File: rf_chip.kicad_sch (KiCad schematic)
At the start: 8 parts, among them IC4 DW3120TR13, Y1 ECS-384-CDX-2482

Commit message: SPI for rf chip DW and MCU, finding a SP8T or SP4T
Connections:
- net DW_SPIDO renamed DW_SPIMISO
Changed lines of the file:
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@@
     )
   )
-  (global_label "DW_SPIDO" (shape bidirectional) (at 48.26 43.18 180) (fields_autoplaced)
+  (global_label "DW_SPIMISO" (shape bidirectional) (at 48.26 43.18 180) (fields_autoplaced)
     (effects (font (size 1.27 1.27)) (justify right))
-    (property "Intersheetrefs" "${INTERSHEET_REFS}" (at 34.7897 43.18 0)
+    (property "Intersheetrefs" "${INTERSHEET_REFS}" (at 32.794 43.18 0)
       (effects (font (size 1.27 1.27)) (justify right) hide)
     )

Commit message: adding all footprints moving onto pcb
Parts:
- C50, C51, C54, C55: footprint (none) -> Capacitor_SMD:C_0603_1608Metric
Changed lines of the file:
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@@
       (effects (font (size 1.27 1.27)) (justify left))
     )
-    (property "Footprint" "" (at 193.04 48.26 0)
+    (property "Footprint" "Capacitor_SMD:C_0603_1608Metric" (at 193.04 48.26 0)
       (effects (font (size 1.27 1.27)) hide)
     )
@@
       (effects (font (size 1.27 1.27)) (justify left))
     )
-    (property "Footprint" "" (at 29.21 29.21 0)
+    (property "Footprint" "Capacitor_SMD:C_0603_1608Metric" (at 29.21 29.21 0)
       (effects (font (size 1.27 1.27)) hide)
     )
@@
       (effects (font (size 1.27 1.27)) (justify right))
     )
-    (property "Footprint" "" (at 210.82 50.8 0)
+    (property "Footprint" "Capacitor_SMD:C_0603_1608Metric" (at 210.82 50.8 0)
       (effects (font (size 1.27 1.27)) hide)
     )
@@
       (effects (font (size 1.27 1.27)) (justify right))
     )
-    (property "Footprint" "" (at 29.21 96.52 0)
+    (property "Footprint" "Capacitor_SMD:C_0603_1608Metric" (at 29.21 96.52 0)
       (effects (font (size 1.27 1.27)) hide)
     )

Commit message: fixed GS_VBUS overtaking the GND symbol error, lesson learned, fixed PCB ratnest
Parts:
- removed AE1, AE2: Antenna, symbol Device:Antenna
- IC4: footprint DW3120TR13 -> dw3120:DW3120TR13
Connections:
- net DW_RF2: now reaches IC4.H11 (RF1)
- net DW_RF1: now reaches IC4.H5 (RF2)
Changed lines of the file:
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@@
+    )
+  )
+  (global_label "DW_RF1" (shape bidirectional) (at 139.7 88.9 0) (fields_autoplaced)
+    (effects (font (size 1.27 1.27)) (justify left))
+    (property "Intersheetrefs" "${INTERSHEET_REFS}" (at 151.0536 88.9 0)
+      (effects (font (size 1.27 1.27)) (justify left) hide)
     )
   )
@@
     (property "Intersheetrefs" "${INTERSHEET_REFS}" (at 36.0597 96.52 0)
       (effects (font (size 1.27 1.27)) (justify right) hide)
+    )
+  )
+  (global_label "DW_RF2" (shape bidirectional) (at 144.78 96.52 0) (fields_autoplaced)
+    (effects (font (size 1.27 1.27)) (justify left))
+    (property "Intersheetrefs" "${INTERSHEET_REFS}" (at 156.1336 96.52 0)
+      (effects (font (size 1.27 1.27)) (justify left) hide)
     )
   )
@@
     )
   )
-  (symbol (lib_id "Device:Antenna") (at 144.78 91.44 0) (unit 1)
-    (in_bom yes) (on_board yes) (dnp no) (fields_autoplaced)
-    (property "Reference" "AE2" (at 147.32 90.805 0)
-      (effects (font (size 1.27 1.27)) (justify left))
-    )
-    (property "Value" "Antenna" (at 147.32 93.345 0)
-      (effects (font (size 1.27 1.27)) (justify left))
-    )
-    (property "Footprint" "" (at 144.78 91.44 0)
-      (effects (font (size 1.27 1.27)) hide)
-    )
-    (property "Datasheet" "~" (at 144.78 91.44 0)
-      (effects (font (size 1.27 1.27)) hide)
-    )
-    (pin "1")
-    (instances
-      (project "radar2"
-        (path "/4b235fed-a05d-46ae-99fd-4a907d865754/40342fd5-2d07-4fe2-a926-1f2842abe411"
-          (reference "AE2") (unit 1)
-        )
-      )
-    )
-  )
   (symbol (lib_id "power:GND") (at 29.21 33.02 0) (unit 1)
     (in_bom yes) (on_board yes) (dnp no) (fields_autoplaced)
@@
     )
   )
-  (symbol (lib_id "Device:Antenna") (at 139.7 83.82 0) (unit 1)
-    (in_bom yes) (on_board yes) (dnp no) (fields_autoplaced)
-    (property "Reference" "AE1" (at 142.24 83.185 0)
-      (effects (font (size 1.27 1.27)) (justify left))
-    )
-    (property "Value" "Antenna" (at 142.24 85.725 0)
-      (effects (font (size 1.27 1.27)) (justify left))
-    )
-    (property "Footprint" "" (at 139.7 83.82 0)
-      (effects (font (size 1.27 1.27)) hide)
-    )
-    (property "Datasheet" "~" (at 139.7 83.82 0)
-      (effects (font (size 1.27 1.27)) hide)
-    )
-    (pin "1")
-    (instances
-      (project "radar2"
-        (path "/4b235fed-a05d-46ae-99fd-4a907d865754/40342fd5-2d07-4fe2-a926-1f2842abe411"
-          (reference "AE1") (unit 1)
-        )
-      )
-    )
-  )
   (symbol (lib_id "power:GND") (at 120.65 109.22 0) (unit 1)
     (in_bom yes) (on_board yes) (dnp no) (fields_autoplaced)
@@
       (effects (font (size 1.27 1.27)))
     )
-    (property "Footprint" "DW3120TR13" (at 115.57 133.02 0)
+    (property "Footprint" "dw3120:DW3120TR13" (at 115.57 133.02 0)
       (effects (font (size 1.27 1.27)) (justify left top) hide)
     )

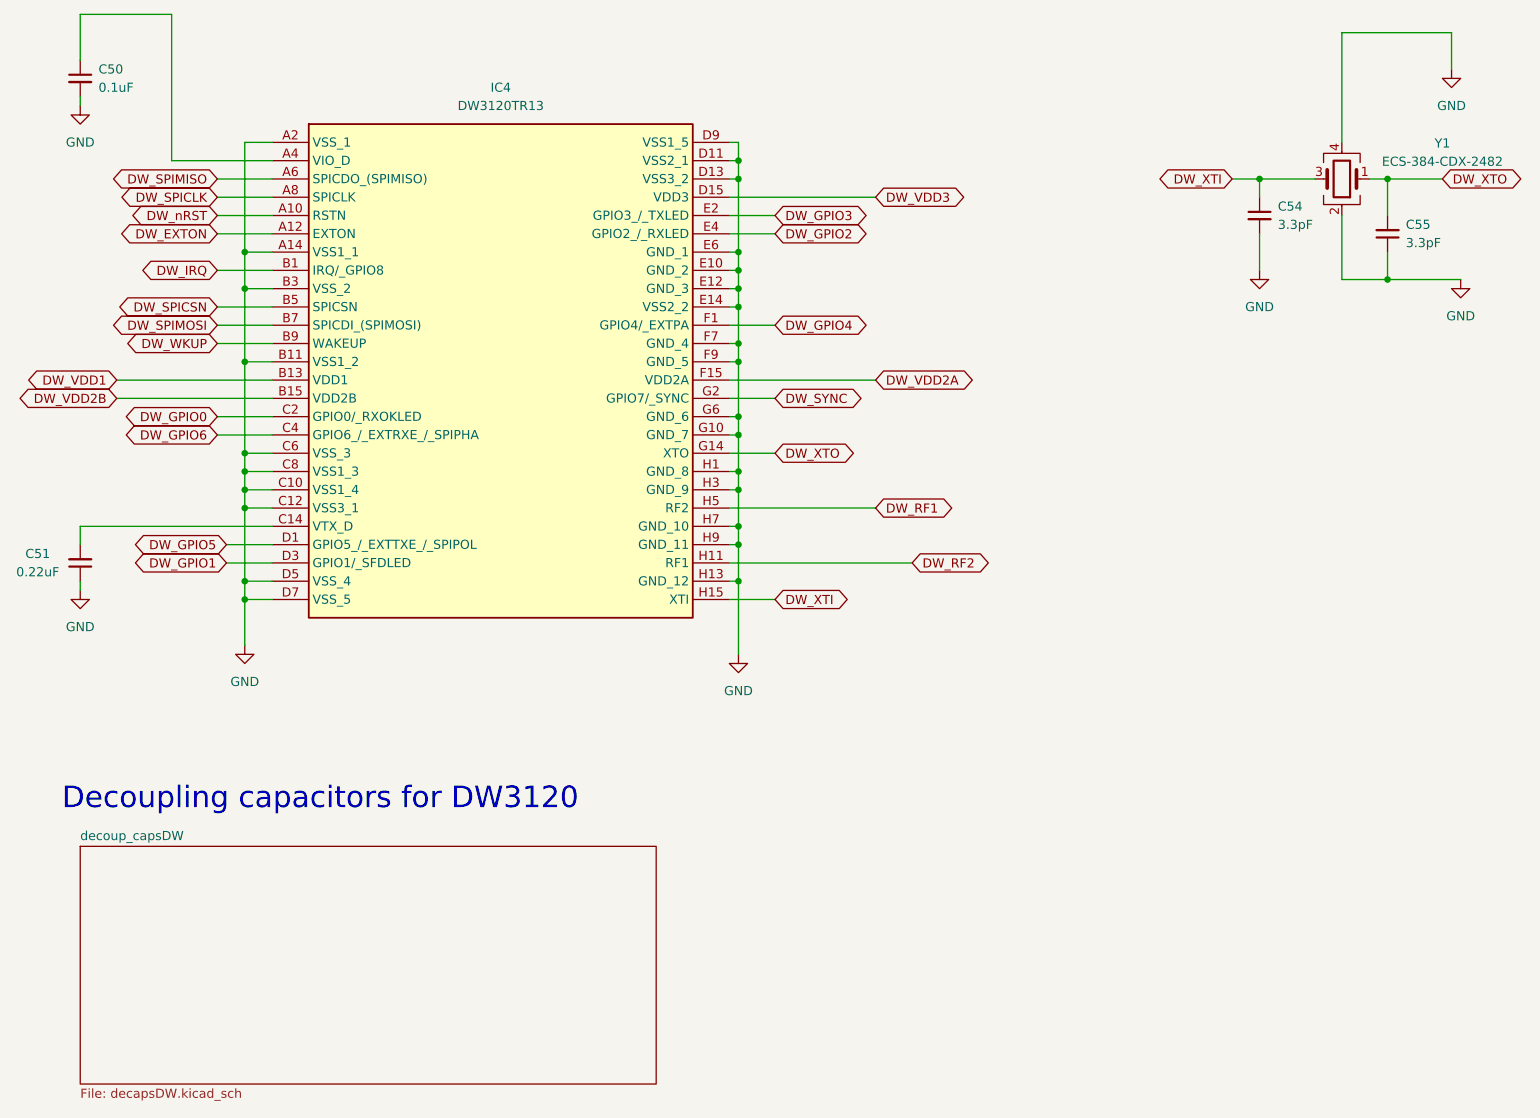
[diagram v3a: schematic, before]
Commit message: adding the .stp files for 3d viewer
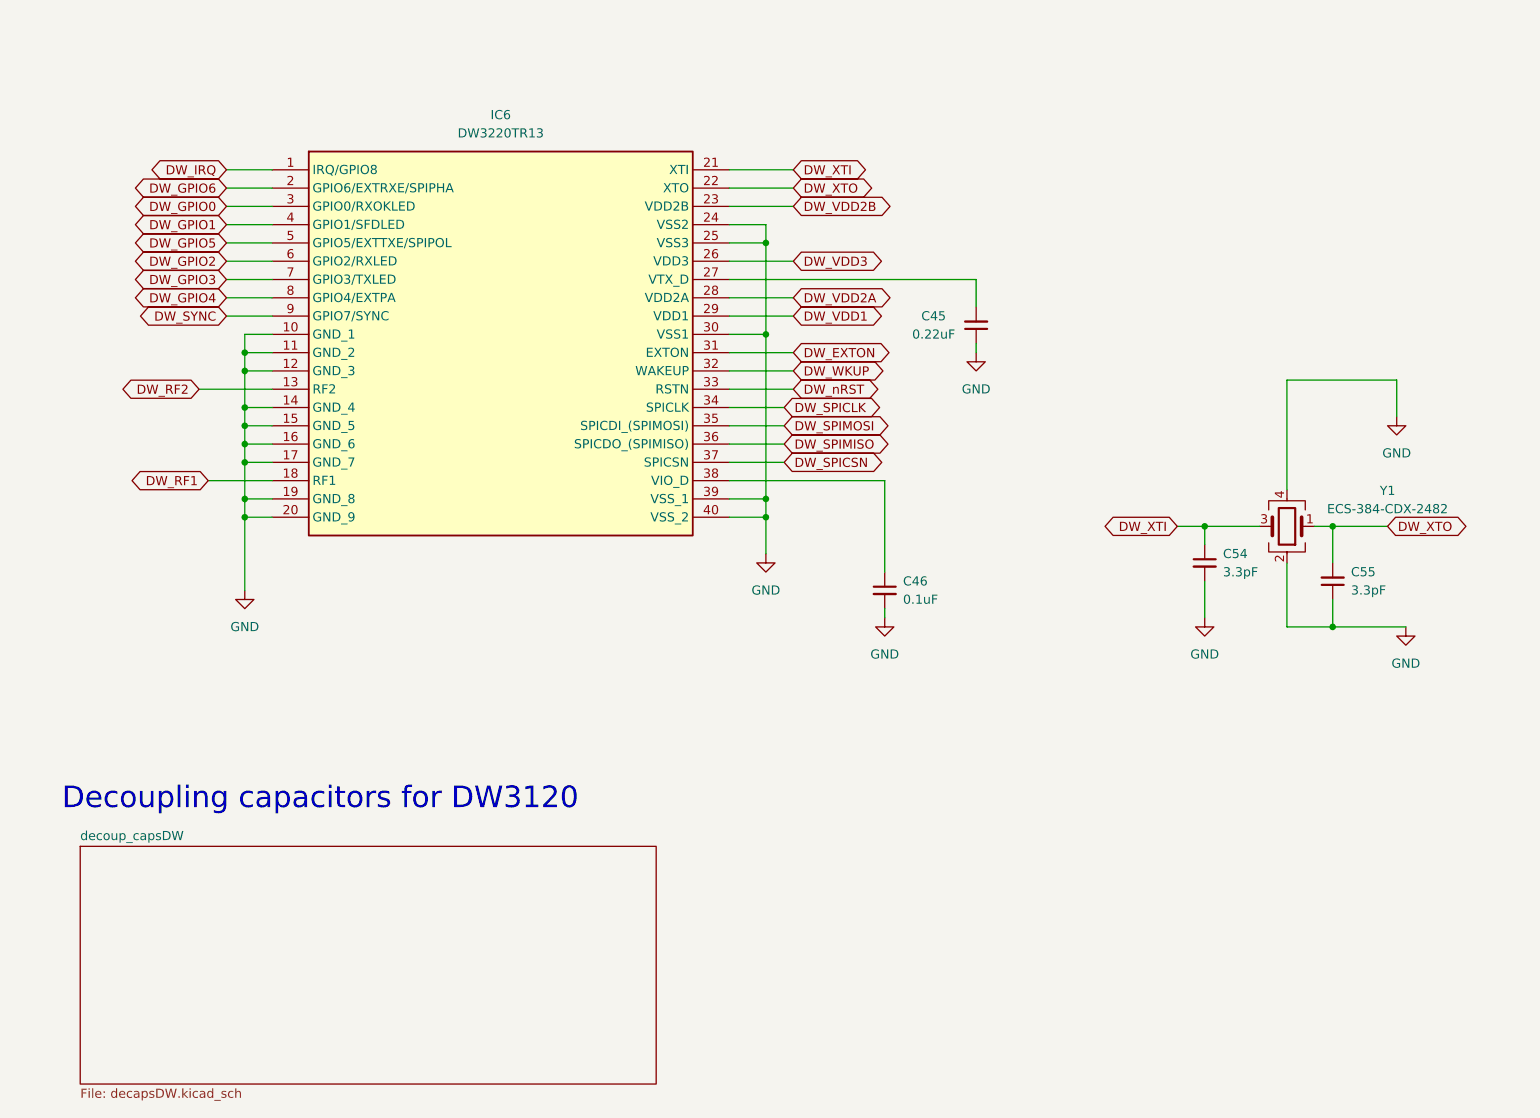
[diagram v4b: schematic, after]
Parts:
- removed C50: 0.1uF, Capacitor_SMD:C_0603_1608Metric, symbol Device:C_Small
- removed C51: 0.22uF, Capacitor_SMD:C_0603_1608Metric, symbol Device:C_Small
- removed IC4: DW3120TR13, dw3120:DW3120TR13, symbol dw31:DW3120TR13
- added C45: 0.22uF, Capacitor_SMD:C_0603_1608Metric, symbol Device:C_Small
- added C46: 0.1uF, Capacitor_SMD:C_0603_1608Metric, symbol Device:C_Small
- added IC6: DW3220TR13, dw3220:DW3220TR13-1, symbol dw32:DW3220TR13
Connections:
- net DW_EXTON: now also IC6.31 (EXTON)
- net DW_GPIO0: now also IC6.3 (GPIO0/RXOKLED)
- net DW_GPIO1: now also IC6.4 (GPIO1/SFDLED)
- net DW_GPIO2: now also IC6.6 (GPIO2/RXLED)
- net DW_GPIO3: now also IC6.7 (GPIO3/TXLED)
- net DW_GPIO4: now also IC6.8 (GPIO4/EXTPA)
- net DW_GPIO5: now also IC6.5 (GPIO5/EXTTXE/SPIPOL)
- net DW_GPIO6: now also IC6.2 (GPIO6/EXTRXE/SPIPHA)
- net DW_IRQ: now also IC6.1 (IRQ/GPIO8)
- net DW_RF1: now also IC6.18 (RF1)
- net DW_RF2: now also IC6.13 (RF2)
- net DW_SPICLK: now also IC6.34 (SPICLK)
- net DW_SPICSN: now also IC6.37 (SPICSN)
- net DW_SPIMISO: now also IC6.36 (SPICDO_(SPIMISO))
- net DW_SPIMOSI: now also IC6.35 (SPICDI_(SPIMOSI))
- net DW_SYNC: now also IC6.9 (GPIO7/SYNC)
- net DW_VDD1: now also IC6.29 (VDD1)
- net DW_VDD2A: now also IC6.28 (VDD2A)
- net DW_VDD2B: now also IC6.23 (VDD2B)
- net DW_VDD3: now also IC6.26 (VDD3)
- net DW_WKUP: now also IC6.32 (WAKEUP)
- net DW_XTI: now also IC6.21 (XTI)
- net DW_XTO: now also IC6.22 (XTO)
- net DW_nRST: now also IC6.33 (RSTN)
- net GND: now also C45.1, C46.2, IC6.10 (GND_1), IC6.11 (GND_2), IC6.12 (GND_3), IC6.14 (GND_4), IC6.15 (GND_5), IC6.16 (GND_6), IC6.17 (GND_7), IC6.19 (GND_8), IC6.20 (GND_9), IC6.24 (VSS2), IC6.25 (VSS3), IC6.30 (VSS1), IC6.39 (VSS_1), IC6.40 (VSS_2)
- new net: C45.2, IC6.27 (VTX_D)
- new net: C46.1, IC6.38 (VIO_D)
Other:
- moved on the sheet: C54, C55, Y1

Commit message: changing sizes of caps from 06 to 04, also using vias on DW spi interfact to stm32
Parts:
- C45, C46, C54, C55: footprint Capacitor_SMD:C_0603_1608Metric -> Capacitor_SMD:C_0402_1005Metric
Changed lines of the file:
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@@
       (effects (font (size 1.27 1.27)) (justify right))
     )
-    (property "Footprint" "Capacitor_SMD:C_0603_1608Metric" (at 153.67 63.5 0)
+    (property "Footprint" "Capacitor_SMD:C_0402_1005Metric" (at 153.67 63.5 0)
       (effects (font (size 1.27 1.27)) hide)
     )
@@
       (effects (font (size 1.27 1.27)) (justify left))
     )
-    (property "Footprint" "Capacitor_SMD:C_0603_1608Metric" (at 185.42 96.52 0)
+    (property "Footprint" "Capacitor_SMD:C_0402_1005Metric" (at 185.42 96.52 0)
       (effects (font (size 1.27 1.27)) hide)
     )
@@
       (effects (font (size 1.27 1.27)) (justify right))
     )
-    (property "Footprint" "Capacitor_SMD:C_0603_1608Metric" (at 203.2 99.06 0)
+    (property "Footprint" "Capacitor_SMD:C_0402_1005Metric" (at 203.2 99.06 0)
       (effects (font (size 1.27 1.27)) hide)
     )
@@
       (effects (font (size 1.27 1.27)) (justify left))
     )
-    (property "Footprint" "Capacitor_SMD:C_0603_1608Metric" (at 140.97 100.33 0)
-      (effects (font (size 1.27 1.27)) hide)
-    )
+    (property "Footprint" "Capacitor_SMD:C_0402_1005Metric" (at 140.97 100.33 0)
+      (effects (font (size 1.27 1.27)) hide)
+    )
